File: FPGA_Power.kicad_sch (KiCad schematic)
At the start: 32 parts, among them U11 LIFCL-40-9BG256C

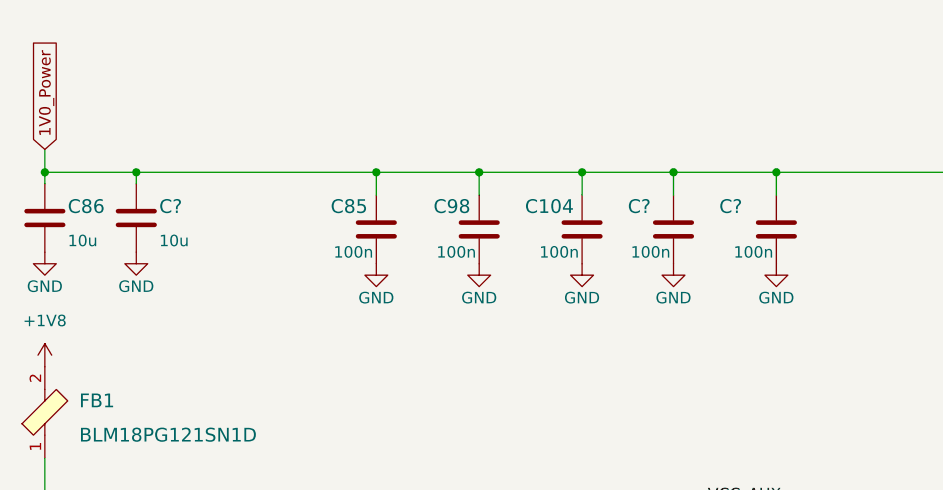
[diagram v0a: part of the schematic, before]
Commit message: Routed flash memory
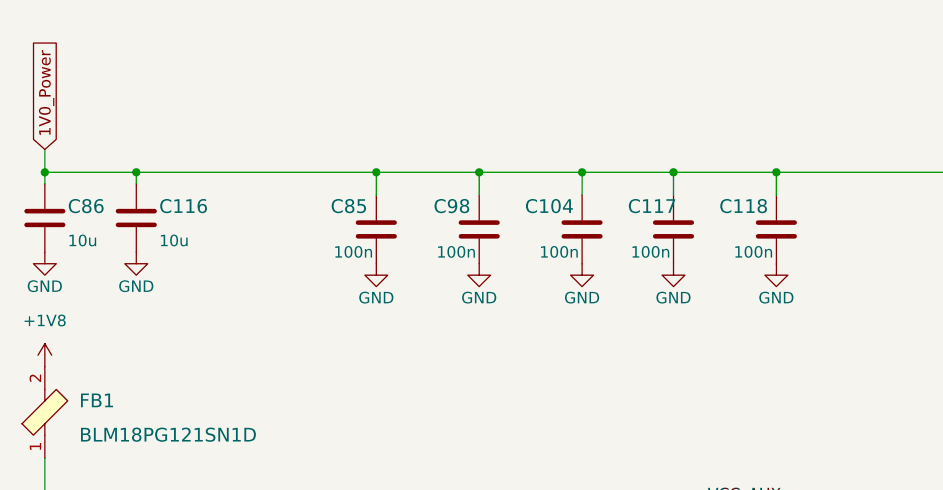
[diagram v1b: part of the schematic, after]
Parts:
- gave numbers to parts that had none: 3
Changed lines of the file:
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@@
   (symbol (lib_id "crosslink-nx-video-converter:C_100n_0402") (at 198.12 53.34 0) (unit 1)
     (in_bom yes) (on_board yes)
-    (property "Reference" "C?" (id 0) (at 193.04 50.8 0)
+    (property "Reference" "C117" (id 0) (at 193.04 50.8 0)
       (effects (font (size 1.524 1.524)) (justify left))
     )
@@
   (symbol (lib_id "crosslink-nx-video-converter:C_100n_0402") (at 209.55 53.34 0) (unit 1)
     (in_bom yes) (on_board yes)
-    (property "Reference" "C?" (id 0) (at 203.2 50.8 0)
+    (property "Reference" "C118" (id 0) (at 203.2 50.8 0)
       (effects (font (size 1.524 1.524)) (justify left))
     )
@@
   (symbol (lib_id "crosslink-nx-video-converter:GND") (at 138.43 55.88 0) (mirror y) (unit 1)
     (in_bom yes) (on_board yes)
-    (property "Reference" "#PWR?" (id 0) (at 138.43 62.23 0)
+    (property "Reference" "#PWR0185" (id 0) (at 138.43 62.23 0)
       (effects (font (size 1.27 1.27)) hide)
     )
@@
   (symbol (lib_id "crosslink-nx-video-converter:GND") (at 209.55 57.15 0) (mirror y) (unit 1)
     (in_bom yes) (on_board yes)
-    (property "Reference" "#PWR?" (id 0) (at 209.55 63.5 0)
+    (property "Reference" "#PWR0260" (id 0) (at 209.55 63.5 0)
       (effects (font (size 1.27 1.27)) hide)
     )
@@
   (symbol (lib_id "crosslink-nx-video-converter:GND") (at 198.12 57.15 0) (mirror y) (unit 1)
     (in_bom yes) (on_board yes)
-    (property "Reference" "#PWR?" (id 0) (at 198.12 63.5 0)
+    (property "Reference" "#PWR0195" (id 0) (at 198.12 63.5 0)
       (effects (font (size 1.27 1.27)) hide)
     )
@@
   (symbol (lib_id "crosslink-nx-video-converter:C_10u_0603") (at 138.43 52.07 0) (unit 1)
     (in_bom yes) (on_board yes)
-    (property "Reference" "C?" (id 0) (at 140.97 50.8 0)
-      (effects (font (size 1.524 1.524)) (justify left))
-    )
+    (property "Reference" "C116" (id 0) (at 140.97 50.8 0)
+      (effects (font (size 1.524 1.524)) (justify left))
+    )

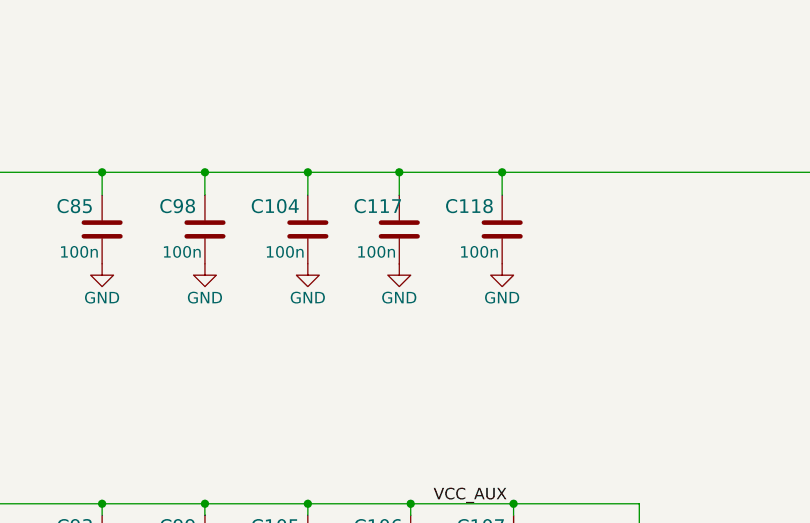
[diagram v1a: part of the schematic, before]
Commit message: Added 0R to low speed FFC signals, moved few testpoints
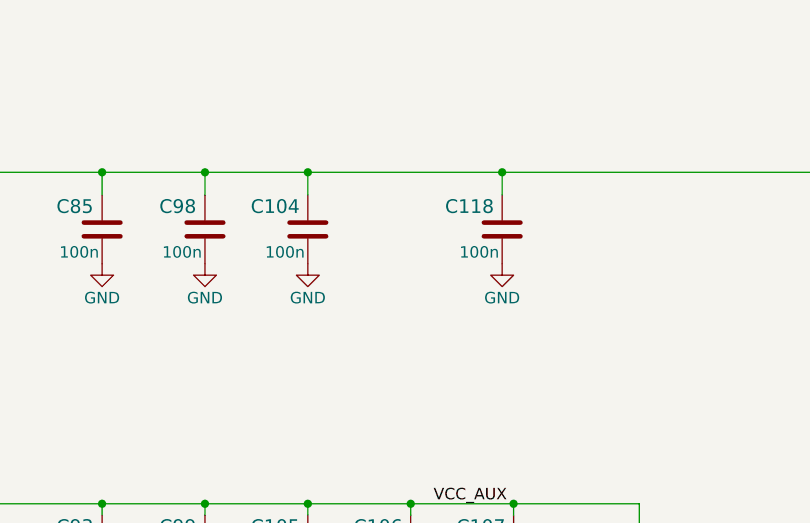
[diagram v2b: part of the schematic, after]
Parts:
- removed C117: C_100n_0402, crosslink-nx-video-converter-footprints:0402-cap, symbol crosslink-nx-video-converter:C_100n_0402
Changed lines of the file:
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@@
   (junction (at 176.53 259.08) (diameter 0) (color 0 0 0 0)
-  )
-  (junction (at 198.12 46.99) (diameter 0) (color 0 0 0 0)
   )
   (junction (at 165.1 83.82) (diameter 0) (color 0 0 0 0)
@@
     (stroke (width 0) (type default) (color 0 0 0 0))
   )
-  (wire (pts (xy 198.12 46.99) (xy 209.55 46.99))
+  (wire (pts (xy 187.96 46.99) (xy 209.55 46.99))
     (stroke (width 0) (type default) (color 0 0 0 0))
   )
@@
     (stroke (width 0) (type default) (color 0 0 0 0))
   )
-  (wire (pts (xy 198.12 46.99) (xy 198.12 49.53))
-    (stroke (width 0) (type default) (color 0 0 0 0))
-  )
   (wire (pts (xy 199.39 83.82) (xy 210.82 83.82))
     (stroke (width 0) (type default) (color 0 0 0 0))
@@
   )
   (wire (pts (xy 222.25 127) (xy 255.27 127))
-    (stroke (width 0) (type default) (color 0 0 0 0))
-  )
-  (wire (pts (xy 187.96 46.99) (xy 198.12 46.99))
     (stroke (width 0) (type default) (color 0 0 0 0))
   )
@@
     )
   )
-  (symbol (lib_id "crosslink-nx-video-converter:C_100n_0402") (at 198.12 53.34 0) (unit 1)
-    (in_bom yes) (on_board yes)
-    (property "Reference" "C117" (id 0) (at 193.04 50.8 0)
-      (effects (font (size 1.524 1.524)) (justify left))
-    )
-    (property "Value" "C_100n_0402" (id 1) (at 198.12 57.15 0)
-      (effects (font (size 1.524 1.524)) hide)
-    )
-    (property "Footprint" "crosslink-nx-video-converter-footprints:0402-cap" (id 2) (at 203.2 48.26 0)
-      (effects (font (size 1.524 1.524)) (justify left) hide)
-    )
-    (property "Datasheet" "" (id 3) (at 198.12 53.34 0)
-      (effects (font (size 1.27 1.27)) hide)
-    )
-    (property "Manufacturer" "Murata" (id 4) (at 203.2 43.18 0)
-      (effects (font (size 1.524 1.524)) (justify left) hide)
-    )
-    (property "MPN" "GRM155R61H104KE14D" (id 5) (at 203.2 45.72 0)
-      (effects (font (size 1.524 1.524)) (justify left) hide)
-    )
-    (property "Val" "100n" (id 6) (at 195.58 55.88 0))
-    (pin "1")
-    (pin "2")
-  )
   (symbol (lib_id "crosslink-nx-video-converter:C_10u_0603") (at 128.27 52.07 0) (unit 1)
     (in_bom yes) (on_board yes)
@@
       (effects (font (size 1.27 1.27)) hide)
     )
-    (pin "1")
-  )
-  (symbol (lib_id "crosslink-nx-video-converter:GND") (at 198.12 57.15 0) (mirror y) (unit 1)
-    (in_bom yes) (on_board yes)
-    (property "Reference" "#PWR0195" (id 0) (at 198.12 63.5 0)
-      (effects (font (size 1.27 1.27)) hide)
-    )
-    (property "Value" "GND" (id 1) (at 198.12 60.96 0))
-    (property "Footprint" "crosslink-nx-video-converter-footprints:" (id 2) (at 198.12 57.15 0)
-      (effects (font (size 1.27 1.27)) hide)
-    )
-    (property "Datasheet" "" (id 3) (at 198.12 57.15 0)
-      (effects (font (size 1.27 1.27)) hide)
-    )

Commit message: Added revision and title to the schematic sheets
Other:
- title: (none) -> CrossLink-NX Video Converter
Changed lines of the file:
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@@
 (kicad_sch (version 20211123) (generator eeschema)
   (paper "A3")
+  (title_block
+    (title "CrossLink-NX Video Converter")
+    (date "2022-10-27")
+    (rev "1.0.0")
+    (comment 1 "www.antmicro.com")
+    (comment 2 "Antmicro Ltd.")
+  )
   (junction (at 252.73 144.78) (diameter 0) (color 0 0 0 0)
   )

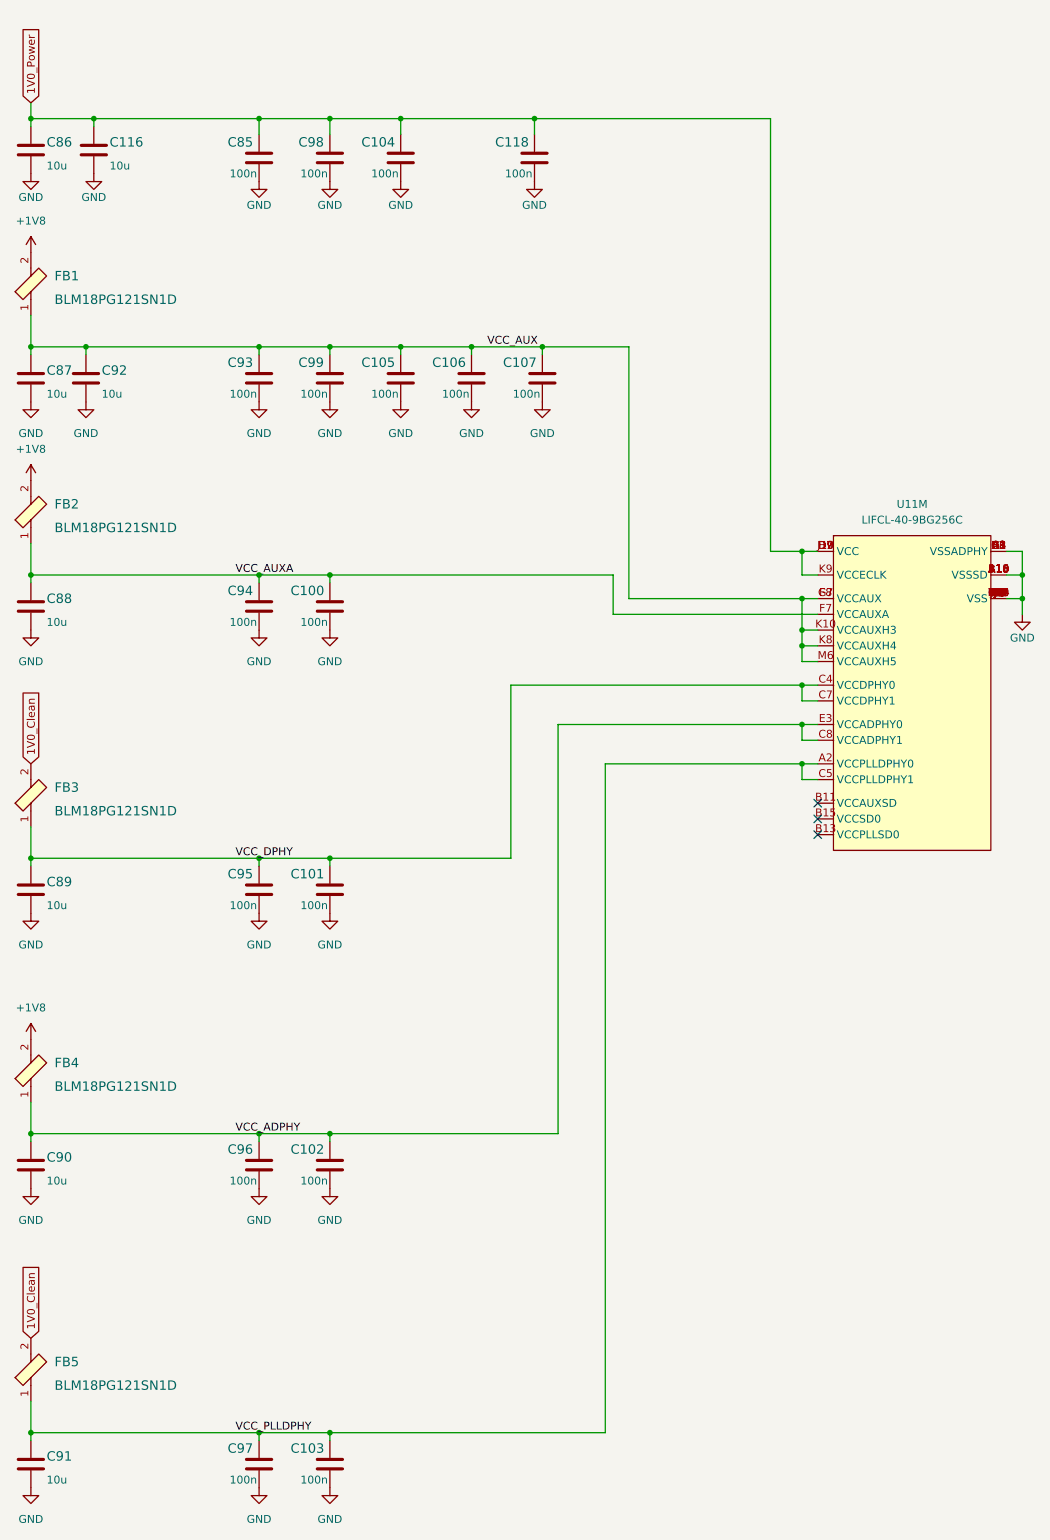
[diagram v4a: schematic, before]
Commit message: Update PCB routing
- apply new DRC
- add FPGA package delay to the high speed traces tunning
- improve GND and power planes
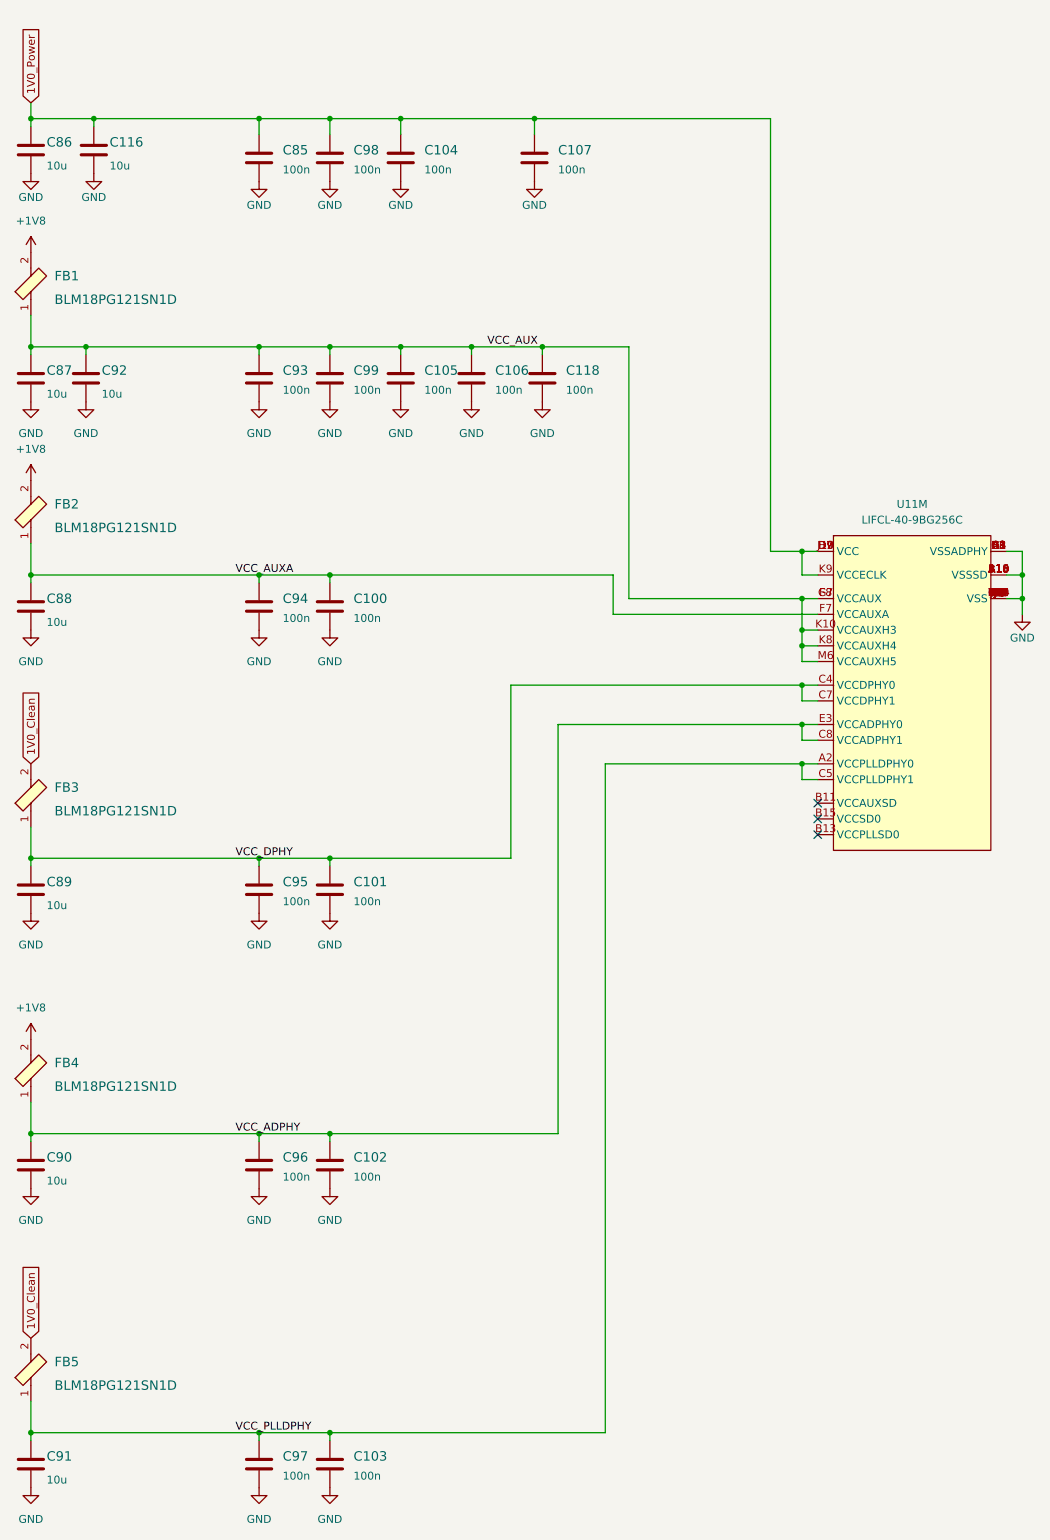
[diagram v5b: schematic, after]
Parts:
- removed C100, C101, C102, C103, C104, C105, C106, C107, C118, C85, C93, C94, C95, C96, C97, C98, C99: C_100n_0402, crosslink-nx-video-converter-footprints:0402-cap, symbol crosslink-nx-video-converter:C_100n_0402
- added C100, C101, C102, C103, C104, C105, C106, C107, C118, C85, C93, C94, C95, C96, C97, C98, C99: C_100n_0201, crosslink-nx-video-converter-footprints:0201-res, symbol crosslink-nx-video-converter:C_100n_0201
- U11: footprint crosslink-nx-video-converter-footprints:BGA-256_16x16_14.0x14.0mm -> crosslink-nx-video-converter-footprints:CrosslinkNX-BGA-256_16x16_14.0x14.0mm
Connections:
- net 1V0_Power: now also C104.1, C107.1, C85.1, C98.1
- net GND: now also C100.2, C101.2, C102.2, C103.2, C104.2, C105.2, C106.2, C107.2, C118.2, C85.2, C93.2, C94.2, C95.2, C96.2, C97.2, C98.2, C99.2
- net VCC_ADPHY: now also C102.1, C96.1
- net VCC_AUX: now also C105.1, C106.1, C118.1, C93.1, C99.1
- net VCC_AUXA: now also C100.1, C94.1
- net VCC_DPHY: now also C101.1, C95.1
- net VCC_PLLDPHY: now also C103.1, C97.1

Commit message: Update project naming convention
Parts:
- C100, C101, C102, C103, C104, C105, C106, C107, C118, C85, C93, C94, C95, C96, C97, C98, C99: footprint crosslink-nx-video-converter-footprints:0201-res -> sdi-mipi-cross-converter-footprints:0201-res; symbol crosslink-nx-video-converter:C_100n_0201 -> sdi-mipi-cross-converter:C_100n_0201
- C116, C86, C87, C88, C89, C90, C91, C92: footprint crosslink-nx-video-converter-footprints:0603-cap -> sdi-mipi-cross-converter-footprints:0603-cap; symbol crosslink-nx-video-converter:C_10u_0603 -> sdi-mipi-cross-converter:C_10u_0603
- FB1, FB2, FB3, FB4, FB5: footprint crosslink-nx-video-converter-footprints:0603-res -> sdi-mipi-cross-converter-footprints:0603-res; symbol crosslink-nx-video-converter:BLM18PG121SN1D -> sdi-mipi-cross-converter:BLM18PG121SN1D
- U11: footprint crosslink-nx-video-converter-footprints:CrosslinkNX-BGA-256_16x16_14.0x14.0mm -> sdi-mipi-cross-converter-footprints:CrosslinkNX-BGA-256_16x16_14.0x14.0mm; symbol crosslink-nx-video-converter:LIFCL-40-9BG256C -> sdi-mipi-cross-converter:LIFCL-40-9BG256C

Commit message: Bump to 1.1.0, update naming
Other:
- title: CrossLink-NX Video Converter -> SDI-MIPI Cross Converter

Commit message: Update U11/LIFCL-40-9BG256C footprint property
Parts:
- U11: footprint sdi-mipi-cross-converter-footprints:CrosslinkNX-BGA-256_16x16_14.0x14.0mm -> sdi-mipi-cross-converter-footprints:BGA-256_16x16_14.0x14.0mm
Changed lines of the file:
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@@
     (property "Reference" "U11" (id 0) (at 270.51 109.22 0))
     (property "Value" "LIFCL-40-9BG256C" (id 1) (at 270.51 111.76 0))
-    (property "Footprint" "sdi-mipi-cross-converter-footprints:CrosslinkNX-BGA-256_16x16_14.0x14.0mm" (id 2) (at 272.415 282.575 0)
+    (property "Footprint" "sdi-mipi-cross-converter-footprints:BGA-256_16x16_14.0x14.0mm" (id 2) (at 272.415 282.575 0)
       (effects (font (size 1.27 1.27)) hide)
     )
